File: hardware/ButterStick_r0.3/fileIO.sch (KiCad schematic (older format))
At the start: 25 parts, among them J2 JST GH Series, J4 MicroSD, U20 PUSB3FR6

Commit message: hw.r0_3: Experiment with buses
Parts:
- R3, R35, R36, R37, R38, R39, R40, R41, R42, R73, R74, R75, R76: footprint pkl_dipol:R_0402 -> Resistor_SMD:R_0402_1005Metric
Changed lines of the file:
@@
 $Descr A4 11693 8268
 encoding utf-8
-Sheet 2 15
+Sheet 11 16
 Title "ButterStick"
 Date "2019-06-14"
@@
 F 0 "R3" V 2593 2250 50  0000 C CNN
 F 1 "1k" V 2684 2250 50  0000 C CNN
-F 2 "pkl_dipol:R_0402" V 2730 2250 50  0001 C CNN
+F 2 "Resistor_SMD:R_0402_1005Metric" V 2730 2250 50  0001 C CNN
 F 3 "" H 2800 2250 50  0001 C CNN
 F 4 "311-1.0KJRCT-ND" H -6500 300 50  0001 C CNN "SN-DK"
@@
 F 0 "R35" V 2593 2600 50  0000 C CNN
 F 1 "1k" V 2684 2600 50  0000 C CNN
-F 2 "pkl_dipol:R_0402" V 2730 2600 50  0001 C CNN
+F 2 "Resistor_SMD:R_0402_1005Metric" V 2730 2600 50  0001 C CNN
 F 3 "" H 2800 2600 50  0001 C CNN
 F 4 "311-1.0KJRCT-ND" H -6500 650 50  0001 C CNN "SN-DK"
@@
 F 0 "R36" V 2593 2950 50  0000 C CNN
 F 1 "1k" V 2684 2950 50  0000 C CNN
-F 2 "pkl_dipol:R_0402" V 2730 2950 50  0001 C CNN
+F 2 "Resistor_SMD:R_0402_1005Metric" V 2730 2950 50  0001 C CNN
 F 3 "" H 2800 2950 50  0001 C CNN
 F 4 "311-1.0KJRCT-ND" H -6500 1000 50  0001 C CNN "SN-DK"
@@
 F 0 "R37" V 2593 3300 50  0000 C CNN
 F 1 "1k" V 2684 3300 50  0000 C CNN
-F 2 "pkl_dipol:R_0402" V 2730 3300 50  0001 C CNN
+F 2 "Resistor_SMD:R_0402_1005Metric" V 2730 3300 50  0001 C CNN
 F 3 "" H 2800 3300 50  0001 C CNN
 F 4 "311-1.0KJRCT-ND" H -6500 1350 50  0001 C CNN "SN-DK"
@@
 F 0 "R38" V 2593 3650 50  0000 C CNN
 F 1 "1k" V 2684 3650 50  0000 C CNN
-F 2 "pkl_dipol:R_0402" V 2730 3650 50  0001 C CNN
+F 2 "Resistor_SMD:R_0402_1005Metric" V 2730 3650 50  0001 C CNN
 F 3 "" H 2800 3650 50  0001 C CNN
 F 4 "311-1.0KJRCT-ND" H -6500 1700 50  0001 C CNN "SN-DK"
@@
 F 0 "R40" V 2593 4000 50  0000 C CNN
 F 1 "1k" V 2684 4000 50  0000 C CNN
-F 2 "pkl_dipol:R_0402" V 2730 4000 50  0001 C CNN
+F 2 "Resistor_SMD:R_0402_1005Metric" V 2730 4000 50  0001 C CNN
 F 3 "" H 2800 4000 50  0001 C CNN
 F 4 "311-1.0KJRCT-ND" H -6500 2050 50  0001 C CNN "SN-DK"
@@
 F 0 "R41" V 2593 4350 50  0000 C CNN
 F 1 "1k" V 2684 4350 50  0000 C CNN
-F 2 "pkl_dipol:R_0402" V 2730 4350 50  0001 C CNN
+F 2 "Resistor_SMD:R_0402_1005Metric" V 2730 4350 50  0001 C CNN
 F 3 "" H 2800 4350 50  0001 C CNN
 F 4 "311-1.0KJRCT-ND" H -6500 2400 50  0001 C CNN "SN-DK"
@@
 F 0 "R42" V 2593 4700 50  0000 C CNN
 F 1 "1k" V 2684 4700 50  0000 C CNN
-F 2 "pkl_dipol:R_0402" V 2730 4700 50  0001 C CNN
+F 2 "Resistor_SMD:R_0402_1005Metric" V 2730 4700 50  0001 C CNN
 F 3 "" H 2800 4700 50  0001 C CNN
 F 4 "311-1.0KJRCT-ND" H -6500 2750 50  0001 C CNN "SN-DK"
@@
 F 0 "R39" V 2593 5350 50  0000 C CNN
 F 1 "1k" V 2684 5350 50  0000 C CNN
-F 2 "pkl_dipol:R_0402" V 2730 5350 50  0001 C CNN
+F 2 "Resistor_SMD:R_0402_1005Metric" V 2730 5350 50  0001 C CNN
 F 3 "" H 2800 5350 50  0001 C CNN
 F 4 "311-1.0KJRCT-ND" H -6500 3400 50  0001 C CNN "SN-DK"
@@
 F 0 "R73" H 6980 4746 50  0000 R CNN
 F 1 "4k7" H 6980 4655 50  0000 R CNN
-F 2 "pkl_dipol:R_0402" V 6980 4700 50  0001 C CNN
+F 2 "Resistor_SMD:R_0402_1005Metric" V 6980 4700 50  0001 C CNN
 F 3 "" H 7050 4700 50  0001 C CNN
 F 4 "RC0402JR-074K7L" H -2250 2750 50  0001 C CNN "PN"
@@
 F 0 "R74" H 6980 5646 50  0000 R CNN
 F 1 "4k7" H 6980 5555 50  0000 R CNN
-F 2 "pkl_dipol:R_0402" V 6980 5600 50  0001 C CNN
+F 2 "Resistor_SMD:R_0402_1005Metric" V 6980 5600 50  0001 C CNN
 F 3 "" H 7050 5600 50  0001 C CNN
 F 4 "RC0402JR-074K7L" H -2250 3650 50  0001 C CNN "PN"
@@
 F 0 "R75" H 7280 4746 50  0000 R CNN
 F 1 "4k7" H 7280 4655 50  0000 R CNN
-F 2 "pkl_dipol:R_0402" V 7280 4700 50  0001 C CNN
+F 2 "Resistor_SMD:R_0402_1005Metric" V 7280 4700 50  0001 C CNN
 F 3 "" H 7350 4700 50  0001 C CNN
 F 4 "RC0402JR-074K7L" H -1950 2750 50  0001 C CNN "PN"
@@
 F 0 "R76" H 7580 4746 50  0000 R CNN
 F 1 "4k7" H 7580 4655 50  0000 R CNN
-F 2 "pkl_dipol:R_0402" V 7580 4700 50  0001 C CNN
+F 2 "Resistor_SMD:R_0402_1005Metric" V 7580 4700 50  0001 C CNN
 F 3 "" H 7650 4700 50  0001 C CNN
 F 4 "RC0402JR-074K7L" H -1650 2750 50  0001 C CNN "PN"

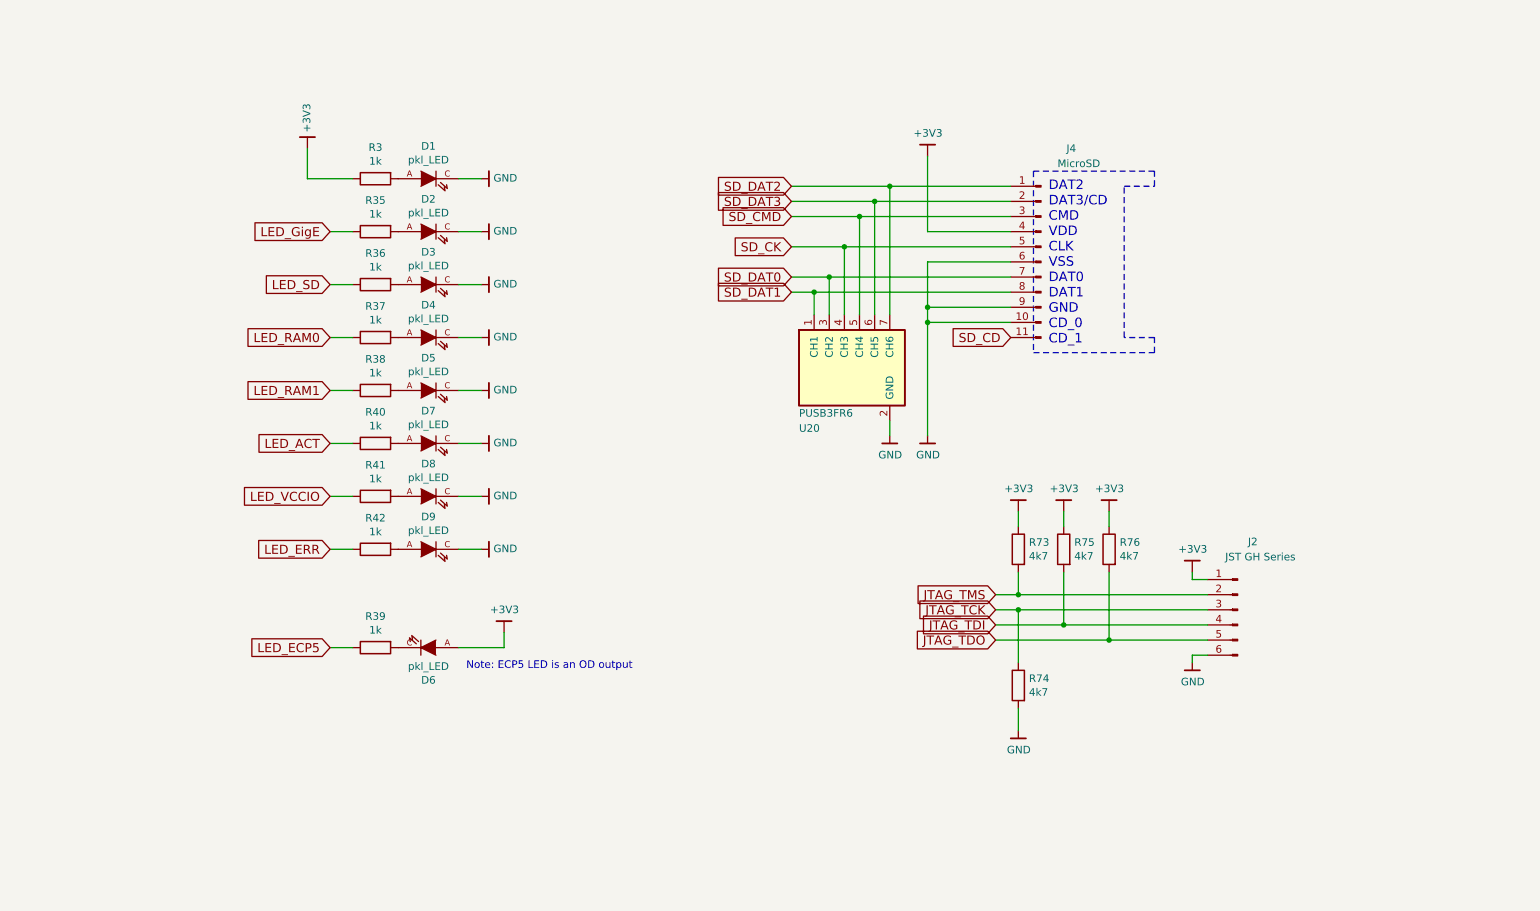
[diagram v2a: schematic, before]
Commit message: hw.r0_3: Update schematics with 85F-5G symbol
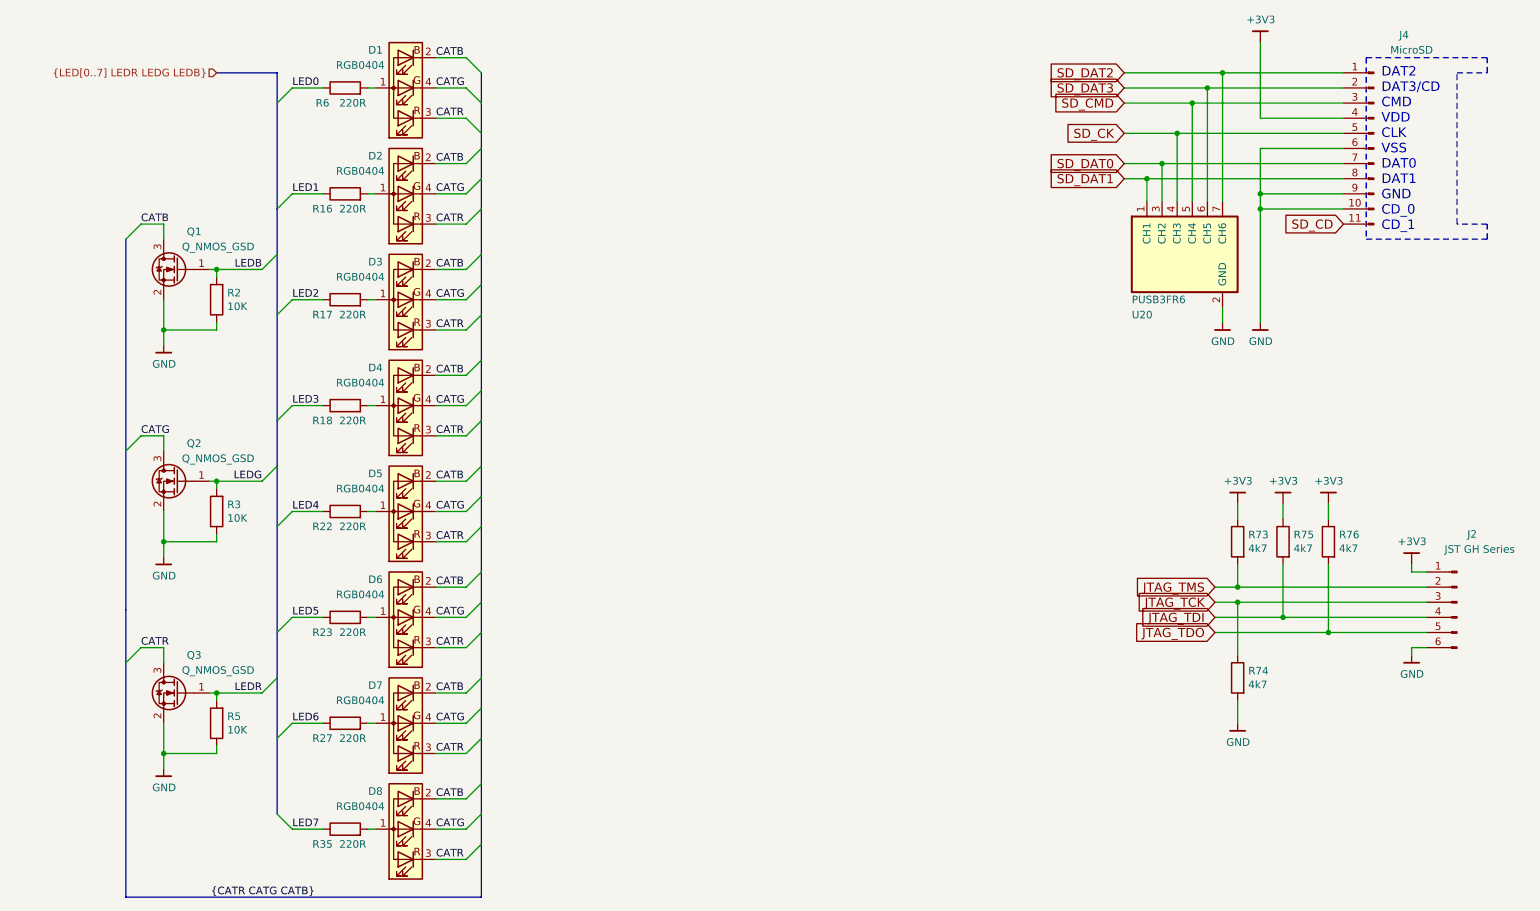
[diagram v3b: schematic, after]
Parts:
- removed D1, D2, D3, D4, D5, D6, D7, D8, D9: pkl_LED, pkl_dipol:D_0603, symbol pkl_device:pkl_LED
- removed R36, R37, R38, R39, R40, R41, R42: 1k, Resistor_SMD:R_0402_1005Metric, symbol Device:R
- added D1, D2, D3, D4, D5, D6, D7, D8: RGB0404, gkl_led:0404LED_RGB, symbol Device:LED_ABRG
- added Q1, Q2, Q3: Q_NMOS_GSD, Package_TO_SOT_SMD:SOT-883, symbol Device:Q_NMOS_GSD
- added R16, R17, R18, R22, R23, R27, R6: 220R, Resistor_SMD:R_0402_1005Metric, symbol Device:R
- added R2, R5: 10K, Resistor_SMD:R_0402_1005Metric, symbol Device:R
- R3: value 1k -> 10K; PN RC0402JR-071KL -> (none); SN-DK 311-1.0KJRCT-ND -> (none)
- R35: value 1k -> 220R; PN RC0402JR-071KL -> (none); SN-DK 311-1.0KJRCT-ND -> (none)
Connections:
- net +3V3: no longer R3.1
- net GND: now also R3.1, Q1.2 (S), Q2.2 (S), Q3.2 (S), R2.1, R5.1
- net LEDG: now reaches R3.2
- net LEDG: now also Q2.1 (G)
- net at R35.2: now also D8.1 (A)
- net LED_GigE renamed LED7
- new net: D1.1 (A), R6.2
- new net: D2.1 (A), R16.2
- new net: D4.1 (A), R18.2
- new net: D3.1 (A), R17.2
- new net: D6.1 (A), R23.2
- new net: D7.1 (A), R27.2
- new net: D5.1 (A), R22.2
- new net CATB: D1.2 (BK), D2.2 (BK), D3.2 (BK), D4.2 (BK), D5.2 (BK), D6.2 (BK), D7.2 (BK), D8.2 (BK), Q1.3 (D)
- new net CATG: D1.4 (GK), D2.4 (GK), D3.4 (GK), D4.4 (GK), D5.4 (GK), D6.4 (GK), D7.4 (GK), D8.4 (GK), Q2.3 (D)
- new net CATR: D1.3 (RK), D2.3 (RK), D3.3 (RK), D4.3 (RK), D5.3 (RK), D6.3 (RK), D7.3 (RK), D8.3 (RK), Q3.3 (D)
- new net LED0: R6.1
- new net LED1: R16.1
- new net LED2: R17.1
- new net LED3: R18.1
- new net LED4: R22.1
- new net LED5: R23.1
- new net LED6: R27.1
- new net LEDB: Q1.1 (G), R2.2
- new net LEDR: Q3.1 (G), R5.2
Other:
- note removed: "Note: ECP5 LED is an OD output"
- moved on the sheet: J2, J4, R73, R74, R75, R76, U20

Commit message: hw.r0_3: Start pin assignments for DDR3
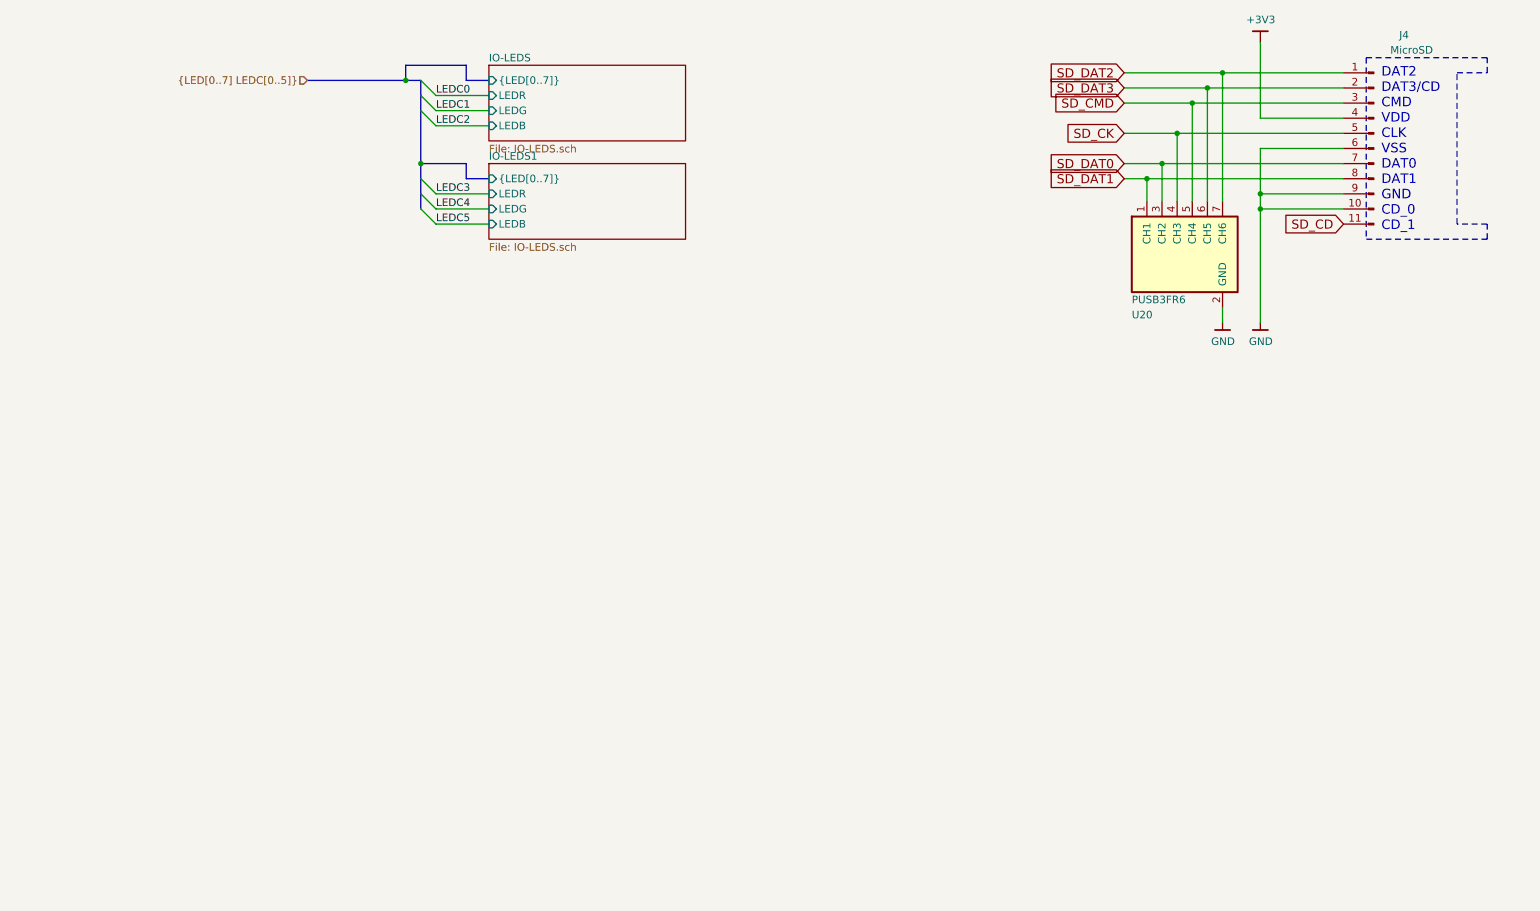
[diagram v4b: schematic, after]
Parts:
- removed D1, D2, D3, D4, D5, D6, D7, D8: RGB0404, gkl_led:0404LED_RGB, symbol Device:LED_ABRG
- removed J2: JST GH Series, Connectors_JST:JST_GH_BM06B-GHS-TBT_06x1.25mm_Straight, symbol Connector:Conn_01x06_Male
- removed Q1, Q2, Q3: Q_NMOS_GSD, Package_TO_SOT_SMD:SOT-883, symbol Device:Q_NMOS_GSD
- removed R16, R17, R18, R22, R23, R27, R35, R6: 220R, Resistor_SMD:R_0402_1005Metric, symbol Device:R
- removed R2, R3, R5: 10K, Resistor_SMD:R_0402_1005Metric, symbol Device:R
- removed R73, R74, R75, R76: 4k7, Resistor_SMD:R_0402_1005Metric, symbol Device:R
